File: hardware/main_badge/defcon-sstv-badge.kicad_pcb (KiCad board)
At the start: 2 copper layers, 223.6 x 130.4 mm, 137 parts, among them J1 Conn_01x02, J10 Micro_SD_Card, J11 Mechanical/Grounds, J12 Mechanical/Grounds, J2 USB4105-GF-A, J3 ILI9341 Display Module, J4 Conn_02x09_Odd_Even, J5 SAO1, J6 SAO2, J7 Conn_01x08_Socket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

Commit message: screen LEDs placed, photo button removed
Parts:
- moved C51 244.1 mm to (2.64, 98.8)
- moved C52 242.2 mm to (2.64, 88.0)
- moved C53 240.9 mm to (2.64, 77.3)
- moved C50 231.1 mm to (18.5, 108.5)
- moved C49 219.1 mm to (31.3, 108.5)
- moved C38 218.8 mm to (18.5, 63.5)
- moved C39 205.9 mm to (31.3, 63.5)
- moved C48 201.0 mm to (44.1, 108.5)
- moved C40 193.0 mm to (44.1, 63.5)
- moved C47 189.0 mm to (57.0, 108.5)
- moved C41 180.2 mm to (57.0, 63.5)
- moved D25 177.9 mm to (2.64, 96.8)
- moved C46 177.1 mm to (69.8, 108.5)
- moved D26 172.9 mm to (2.64, 86.0)
- moved D24 171.4 mm to (18.5, 110.5)
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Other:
- board size 223.6 x 130.4 mm -> 120 x 120 mm

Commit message: main badge final updates
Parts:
- removed SW6: SW_SPST, Button_Switch_THT:SW_PUSH-12mm
- D10, D11, D2, D3, D4, D5, D6, D7, D8, D9: footprint LED_SMD:LED_WS2812B-2020_PLCC4_2.0x2.0mm -> LED_SMD:LED_WS2812B_PLCC4_5.0x5.0mm_P3.2mm
- moved C28 275.3 mm to (-21.8, -49.5), turned to 45 degrees
- moved C29 263.7 mm to (-12.3, -39.9), turned to 45 degrees
- moved C30 252.0 mm to (-2.66, -30.3), turned to 45 degrees
- moved D2 243.9 mm to (-25.4, -53.0), turned to 45 degrees
- moved C31 240.4 mm to (6.95, -20.7), turned to 45 degrees
- moved D3 234.0 mm to (-15.8, -43.4), turned to 45 degrees
- moved C32 228.8 mm to (16.6, -11.1), turned to 45 degrees
- moved D4 224.1 mm to (-6.20, -33.8), turned to 45 degrees
- moved D5 214.2 mm to (3.42, -24.2), turned to 45 degrees
- moved D6 204.3 mm to (13.0, -14.6), turned to 45 degrees
- moved D7 147.9 mm to (146.3, -53.0), turned to -45 degrees
- moved D8 147.7 mm to (138.7, -43.4), turned to -45 degrees
- moved C37 146.8 mm to (106.3, -11.1), turned to -45 degrees
- moved C33 143.8 mm to (142.8, -49.5), turned to -45 degrees
- moved C34 143.1 mm to (135.2, -39.9), turned to -45 degrees
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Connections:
- U1 pad 53: PHOTO -> unconnected-(U1-GPIO42/ADC2-Pad53)
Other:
- board size 120 x 120 mm -> 186.9 x 180.8 mm
- board text added: "HRV SSTV BADGE Rev 0.1 SAY CHEESE! https://hamvillage.org"

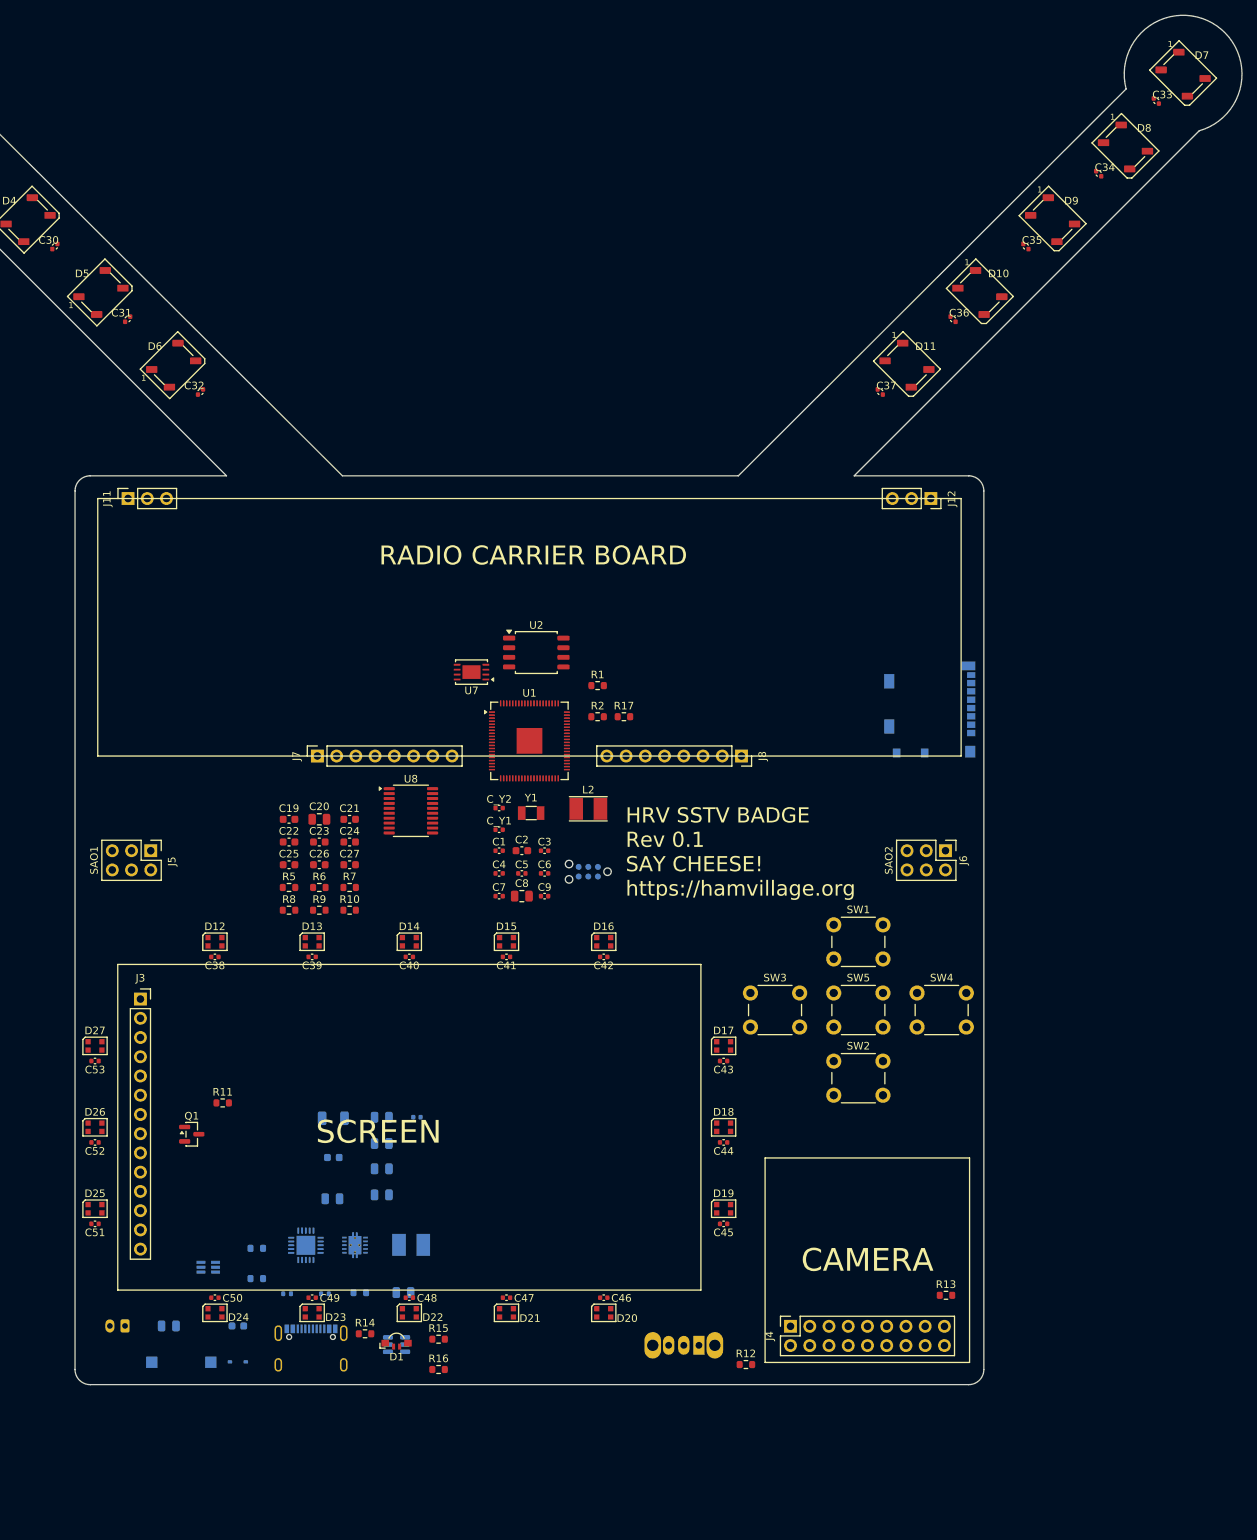
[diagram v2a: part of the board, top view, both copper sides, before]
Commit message: update the PCB for tv cabinet feet
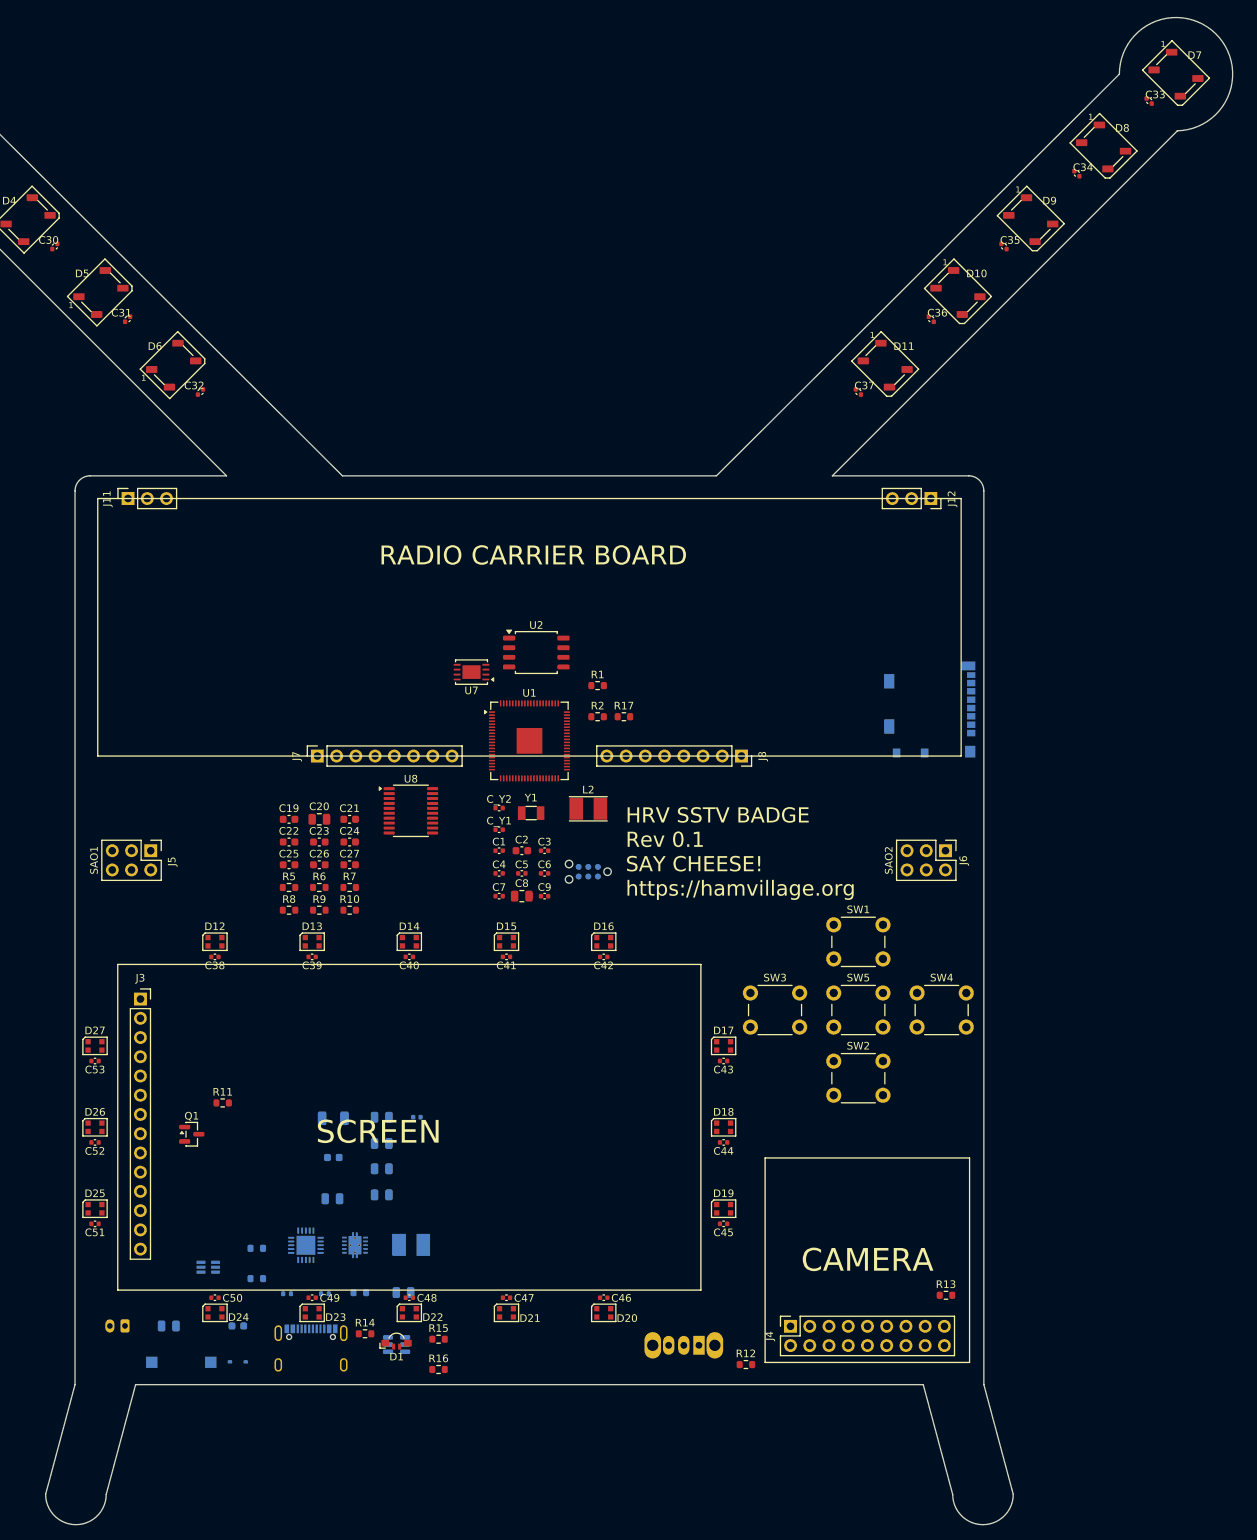
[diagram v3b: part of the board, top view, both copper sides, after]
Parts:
- moved C35 2.89 mm to (122.7, -30.3)
- moved D10 2.89 mm to (116.6, -24.2)
- moved C37 2.89 mm to (103.4, -11.1)
- moved D8 2.89 mm to (135.8, -43.4)
- moved C36 2.88 mm to (113.0, -20.7)
- moved D9 2.88 mm to (126.2, -33.8)
- moved C34 2.88 mm to (132.3, -39.9)
- moved D11 2.88 mm to (107.0, -14.6)
- moved C33 0.94 mm to (141.8, -49.5)
- moved D7 0.94 mm to (145.4, -53.0)
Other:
- board size 186.9 x 180.8 mm -> 185.7 x 199 mm
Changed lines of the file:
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@@
 	(footprint "LED_SMD:LED_WS2812B_PLCC4_5.0x5.0mm_P3.2mm"
 		(layer "F.Cu")
-		(at 109.85 -14.61 -45)
+		(at 106.97 -14.61 -45)
 		(descr "5.0mm x 5.0mm Addressable RGB LED NeoPixel, https://cdn-shop.adafruit.com/datasheets/WS2812B.pdf")
 		(tags "LED RGB NeoPixel PLCC-4 5050")
@@
 	(footprint "Capacitor_SMD:C_0402_1005Metric"
 		(layer "F.Cu")
-		(at 106.32 -11.07 -45)
+		(at 103.43 -11.07 -45)
 		(descr "Capacitor SMD 0402 (1005 Metric), square (rectangular) end terminal, IPC-7351 nominal, (Body size source: IPC-SM-782 page 76, https://www.pcb-3d.com/wordpress/wp-content/uploads/ipc-sm-782a_amendment_1_and_2.pdf), generated with kicad-footprint-generator")
 		(tags "capacitor")
@@
 	(footprint "Capacitor_SMD:C_0402_1005Metric"
 		(layer "F.Cu")
-		(at 135.16 -39.89 -45)
+		(at 132.28 -39.89 -45)
 		(descr "Capacitor SMD 0402 (1005 Metric), square (rectangular) end terminal, IPC-7351 nominal, (Body size source: IPC-SM-782 page 76, https://www.pcb-3d.com/wordpress/wp-content/uploads/ipc-sm-782a_amendment_1_and_2.pdf), generated with kicad-footprint-generator")
 		(tags "capacitor")
@@
 	(footprint "Capacitor_SMD:C_0402_1005Metric"
 		(layer "F.Cu")
-		(at 142.77 -49.49 -45)
+		(at 141.83 -49.49 -45)
 		(descr "Capacitor SMD 0402 (1005 Metric), square (rectangular) end terminal, IPC-7351 nominal, (Body size source: IPC-SM-782 page 76, https://www.pcb-3d.com/wordpress/wp-content/uploads/ipc-sm-782a_amendment_1_and_2.pdf), generated with kicad-footprint-generator")
 		(tags "capacitor")
@@
 	(footprint "Capacitor_SMD:C_0402_1005Metric"
 		(layer "F.Cu")
-		(at 115.93 -20.68 -45)
+		(at 113.05 -20.68 -45)
 		(descr "Capacitor SMD 0402 (1005 Metric), square (rectangular) end terminal, IPC-7351 nominal, (Body size source: IPC-SM-782 page 76, https://www.pcb-3d.com/wordpress/wp-content/uploads/ipc-sm-782a_amendment_1_and_2.pdf), generated with kicad-footprint-generator")
 		(tags "capacitor")
@@
 	(footprint "LED_SMD:LED_WS2812B_PLCC4_5.0x5.0mm_P3.2mm"
 		(layer "F.Cu")
-		(at 146.31 -53.03 -45)
+		(at 145.37 -53.03 -45)
 		(descr "5.0mm x 5.0mm Addressable RGB LED NeoPixel, https://cdn-shop.adafruit.com/datasheets/WS2812B.pdf")
 		(tags "LED RGB NeoPixel PLCC-4 5050")
@@
 	(footprint "LED_SMD:LED_WS2812B_PLCC4_5.0x5.0mm_P3.2mm"
 		(layer "F.Cu")
-		(at 119.47 -24.21 -45)
+		(at 116.58 -24.21 -45)
 		(descr "5.0mm x 5.0mm Addressable RGB LED NeoPixel, https://cdn-shop.adafruit.com/datasheets/WS2812B.pdf")
 		(tags "LED RGB NeoPixel PLCC-4 5050")
@@
 	(footprint "LED_SMD:LED_WS2812B_PLCC4_5.0x5.0mm_P3.2mm"
 		(layer "F.Cu")
-		(at 129.08 -33.82 -45)
+		(at 126.2 -33.82 -45)
 		(descr "5.0mm x 5.0mm Addressable RGB LED NeoPixel, https://cdn-shop.adafruit.com/datasheets/WS2812B.pdf")
 		(tags "LED RGB NeoPixel PLCC-4 5050")
@@
 	(footprint "LED_SMD:LED_WS2812B_PLCC4_5.0x5.0mm_P3.2mm"
 		(layer "F.Cu")
-		(at 138.7 -43.42 -45)
+		(at 135.81 -43.42 -45)
 		(descr "5.0mm x 5.0mm Addressable RGB LED NeoPixel, https://cdn-shop.adafruit.com/datasheets/WS2812B.pdf")
 		(tags "LED RGB NeoPixel PLCC-4 5050")
@@
 	(footprint "Capacitor_SMD:C_0402_1005Metric"
 		(layer "F.Cu")
-		(at 125.55 -30.28 -45)
+		(at 122.66 -30.28 -45)
 		(descr "Capacitor SMD 0402 (1005 Metric), square (rectangular) end terminal, IPC-7351 nominal, (Body size source: IPC-SM-782 page 76, https://www.pcb-3d.com/wordpress/wp-content/uploads/ipc-sm-782a_amendment_1_and_2.pdf), generated with kicad-footprint-generator")
 		(tags "capacitor")
@@
 	)
 	(gr_line
-		(start 118 120)
-		(end 2 120)
+		(start 112 120)
+		(end 8 120)
 		(stroke
 			(width 0.05)
@@
 		(layer "Edge.Cuts")
 	)
-	(gr_arc
-		(start 2 120)
-		(mid 0.585786 119.414214)
-		(end 0 118)
+	(gr_line
+		(start 8 120)
+		(end 4.118 134.489)
 		(stroke
 			(width 0.05)
@@
 	)
 	(gr_arc
-		(start 138.784864 -51.078289)
-		(mid 150.173298 -59.779803)
-		(end 148.434609 -45.553428)
+		(start 137.892835 -53.033002)
+		(mid 150.599675 -58.38483)
+		(end 145.5524 -45.553975)
 		(stroke
 			(width 0.05)
@@
 	)
 	(gr_line
-		(start 102.881181 0)
-		(end 148.434609 -45.553428)
+		(start 99.998425 0)
+		(end 145.5524 -45.553975)
 		(stroke
 			(width 0.05)
@@
 	)
 	(gr_line
-		(start 138.784864 -51.078289)
-		(end 87.582429 0)
+		(start 137.892835 -53.033002)
+		(end 84.694 0)
 		(stroke
 			(width 0.05)
@@
 	(gr_line
 		(start 120 2)
-		(end 120 118)
+		(end 120 120)
+		(stroke
+			(width 0.05)
+			(type default)
+		)
+		(layer "Edge.Cuts")
+	)
+	(gr_arc
+		(start 4.118 134.489)
+		(mid 0.118 138.489)
+		(end -3.882 134.489)
+		(stroke
+			(width 0.05)
+			(type default)
+		)
+		(layer "Edge.Cuts")
+	)
+	(gr_line
+		(start -3.882 134.489)
+		(end 0 120)
+		(stroke
+			(width 0.05)
+			(type default)
+		)
+		(layer "Edge.Cuts")
+	)
+	(gr_arc
+		(start 123.882 134.489)
+		(mid 119.882 138.489)
+		(end 115.882 134.489)
+		(stroke
+			(width 0.05)
+			(type default)
+		)
+		(layer "Edge.Cuts")
+	)
+	(gr_line
+		(start 115.882 134.489)
+		(end 112 120)
 		(stroke
 			(width 0.05)
@@
 	(gr_line
 		(start 35.306 0)
-		(end 87.582429 0)
+		(end 84.694 0)
 		(stroke
 			(width 0.05)
@@
 	)
 	(gr_line
-		(start 102.881181 0)
+		(start 99.998425 0)
 		(end 118 0)
 		(stroke
@@
 		(layer "Edge.Cuts")
 	)
-	(gr_arc
-		(start 120 118)
-		(mid 119.414214 119.414214)
-		(end 118 120)
+	(gr_line
+		(start 120 120)
+		(end 123.882 134.489)
 		(stroke
 			(width 0.05)
@@
 	)
 	(gr_line
-		(start 0 118)
+		(start 0 120)
 		(end 0 2)
 		(stroke

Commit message: inital power cap placement
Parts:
- moved C1 28.5 mm to (72.9, 26.5)
- moved L2 16.1 mm to (68.9, 27.9)
- moved R1 6.38 mm to (67.8, 21.4)
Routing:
- net Net-(U1-VREG_FB): track 0.00 -> 15.1 mm
- net Net-(U1-VREG_LX): track 0.00 -> 5.49 mm
- net GND: track 0.00 -> 0.15 mm, vias 0 -> 1
- added copper zone on In2.Cu, net +3V3
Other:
- copper layers 2 -> 4
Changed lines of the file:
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@@
 	(generator_version "9.0")
 	(general
-		(thickness 1.6)
+		(thickness 0.19)
 		(legacy_teardrops no)
 	)
@@
 	(layers
 		(0 "F.Cu" signal)
+		(4 "In1.Cu" power "GND")
+		(6 "In2.Cu" power "PWR")
 		(2 "B.Cu" signal)
 		(9 "F.Adhes" user "F.Adhesive")
@@
 	)
 	(setup
+		(stackup
+			(layer "F.SilkS"
+				(type "Top Silk Screen")
+			)
+			(layer "F.Paste"
+				(type "Top Solder Paste")
+			)
+			(layer "F.Mask"
+				(type "Top Solder Mask")
+				(thickness 0.01)
+			)
+			(layer "F.Cu"
+				(type "copper")
+				(thickness 0.035)
+			)
+			(layer "dielectric 1"
+				(type "prepreg")
+				(thickness 0.01)
+				(material "FR4")
+				(epsilon_r 4.5)
+				(loss_tangent 0.02)
+			)
+			(layer "In1.Cu"
+				(type "copper")
+				(thickness 0.035)
+			)
+			(layer "dielectric 2"
+				(type "core")
+				(thickness 0.01)
+				(material "FR4")
+				(epsilon_r 4.5)
+				(loss_tangent 0.02)
+			)
+			(layer "In2.Cu"
+				(type "copper")
+				(thickness 0.035)
+			)
+			(layer "dielectric 3"
+				(type "prepreg")
+				(thickness 0.01)
+				(material "FR4")
+				(epsilon_r 4.5)
+				(loss_tangent 0.02)
+			)
+			(layer "B.Cu"
+				(type "copper")
+				(thickness 0.035)
+			)
+			(layer "B.Mask"
+				(type "Bottom Solder Mask")
+				(thickness 0.01)
+			)
+			(layer "B.Paste"
+				(type "Bottom Solder Paste")
+			)
+			(layer "B.SilkS"
+				(type "Bottom Silk Screen")
+			)
+			(copper_finish "None")
+			(dielectric_constraints no)
+		)
 		(pad_to_mask_clearance 0)
 		(allow_soldermask_bridges_in_footprints no)
@@
 	(footprint "Inductor_SMD:L_Taiyo-Yuden_NR-30xx_HandSoldering"
 		(layer "F.Cu")
-		(at 67.77 43.97)
+		(at 68.9384 27.8664)
 		(descr "Inductor, Taiyo Yuden, NR series, Taiyo-Yuden_NR-30xx, 3.0mmx3.0mm")
 		(tags "inductor taiyo-yuden nr smd")
@@
 	(footprint "Resistor_SMD:R_0603_1608Metric"
 		(layer "F.Cu")
-		(at 69 27.7)
+		(at 67.755 21.4376)
 		(descr "Resistor SMD 0603 (1608 Metric), square (rectangular) end terminal, IPC-7351 nominal, (Body size source: IPC-SM-782 page 72, https://www.pcb-3d.com/wordpress/wp-content/uploads/ipc-sm-782a_amendment_1_and_2.pdf), generated with kicad-footprint-generator")
 		(tags "resistor")
@@
 	(footprint "Capacitor_SMD:C_0402_1005Metric"
 		(layer "F.Cu")
-		(at 56 49.5)
+		(at 72.926 26.5176)
 		(descr "Capacitor SMD 0402 (1005 Metric), square (rectangular) end terminal, IPC-7351 nominal, (Body size source: IPC-SM-782 page 76, https://www.pcb-3d.com/wordpress/wp-content/uploads/ipc-sm-782a_amendment_1_and_2.pdf), generated with kicad-footprint-generator")
 		(tags "capacitor")
 		(property "Reference" "C1"
-			(at 0 -1.16 0)
+			(at 0.028 1.2192 0)
 			(layer "F.SilkS")
 			(effects
@@
 		)
 	)
+	(segment
+		(start 64.97138 26.1654)
+		(end 72.0938 26.1654)
+		(width 0.2)
+		(layer "F.Cu")
+		(net 1)
+	)
+	(segment
+		(start 71.8872 26.5176)
+		(end 72.446 26.5176)
+		(width 0.2)
+		(layer "F.Cu")
+		(net 1)
+	)
+	(segment
+		(start 62.2 28.93678)
+		(end 64.97138 26.1654)
+		(width 0.2)
+		(layer "F.Cu")
+		(net 1)
+	)
+	(segment
+		(start 70.5384 27.8664)
+		(end 71.8872 26.5176)
+		(width 0.2)
+		(layer "F.Cu")
+		(net 1)
+	)
+	(segment
+		(start 72.0938 26.1654)
+		(end 72.446 26.5176)
+		(width 0.2)
+		(layer "F.Cu")
+		(net 1)
+	)
+	(segment
+		(start 62.2 30.05)
+		(end 62.2 28.93678)
+		(width 0.2)
+		(layer "F.Cu")
+		(net 1)
+	)
+	(segment
+		(start 73.406 26.5176)
+		(end 73.406 26.67)
+		(width 0.2)
+		(layer "F.Cu")
+		(net 2)
+	)
+	(via
+		(at 73.406 26.5176)
+		(size 0.6)
+		(drill 0.3)
+		(layers "F.Cu" "B.Cu")
+		(net 2)
+	)
+	(segment
+		(start 63 29.622936)
+		(end 64.756536 27.8664)
+		(width 0.2)
+		(layer "F.Cu")
+		(net 104)
+	)
+	(segment
+		(start 63 30.05)
+		(end 63 29.622936)
+		(width 0.2)
+		(layer "F.Cu")
+		(net 104)
+	)
+	(segment
+		(start 64.756536 27.8664)
+		(end 67.3384 27.8664)
+		(width 0.2)
+		(layer "F.Cu")
+		(net 104)
+	)
+	(zone
+		(net 3)
+		(net_name "+3V3")
+		(layer "In2.Cu")
+		(hatch edge 0.5)
+		(connect_pads
+			(clearance 0.5)
+		)
+		(min_thickness 0.25)
+		(filled_areas_thickness no)
+		(fill yes
+			(thermal_gap 0.5)
+			(thermal_bridge_width 0.5)
+		)
+		(polygon
+			(pts
+				(xy -45.212 148.2344) (xy 163.2204 148.2344) (xy 163.576 -72.7964) (xy -42.0116 -75.6412) (xy -46.3296 147.8788)
+			)
+		)
+	)

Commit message: most of the load capacitors
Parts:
- moved C3 21.7 mm to (57.8, 28.2), turned to 90 degrees
- moved C7 20.0 mm to (66.9, 38.8)
- moved C4 19.9 mm to (53.0, 32.8), turned to 180 degrees
- moved C2 19.9 mm to (67.6, 31.6)
- moved C5 16.8 mm to (53.1, 36.8), turned to 180 degrees
- moved C6 11.6 mm to (58.9, 41.3), turned to 180 degrees
- moved C_Y2 7.48 mm to (63.4, 45.0), turned to 90 degrees
- moved C_Y1 5.19 mm to (60.9, 45.0), turned to 90 degrees
- moved R17 3.75 mm to (75.5, 34.1)
- moved R2 3.75 mm to (72.0, 34.1)
- moved Y1 3.18 mm to (62.1, 42.0)
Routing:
- net GND: track 0.15 -> 11.9 mm, vias 1 -> 18
- net +3V3: track 0.00 -> 9.44 mm
- net Net-(U1-XOUT): track 0.00 -> 6.80 mm
- net Net-(U1-XIN): track 0.00 -> 5.05 mm
